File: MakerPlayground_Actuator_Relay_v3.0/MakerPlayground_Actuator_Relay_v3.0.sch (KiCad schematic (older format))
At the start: 7 parts, among them J1 Conn_01x04, J2 Terminal Block, J3 Terminal Block, K1 SANYOU_SRD_Form_C, Q1 Q_NPN_BEC

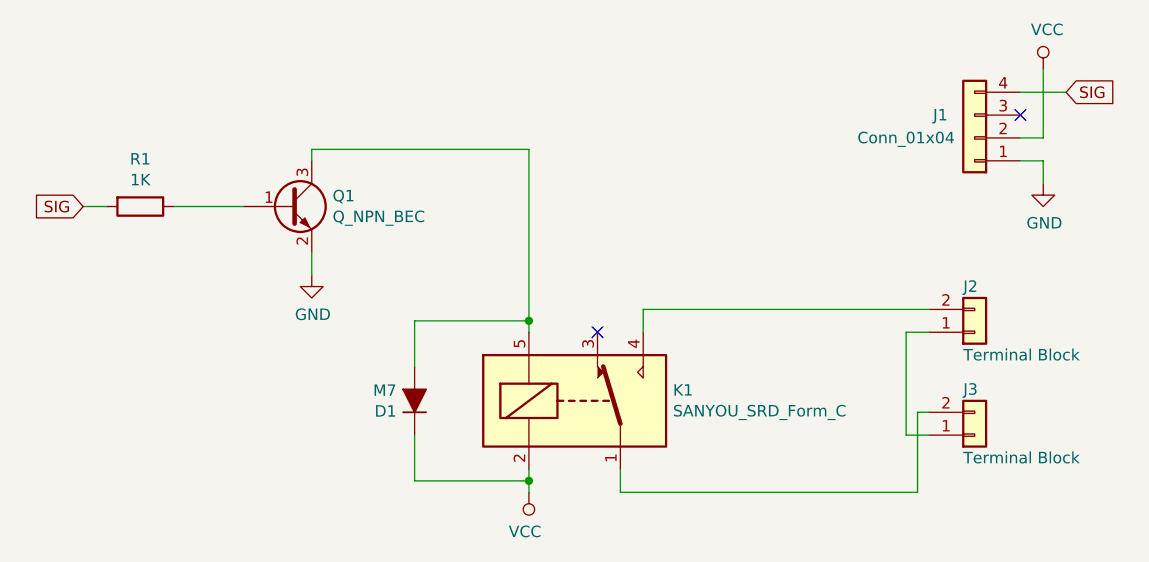
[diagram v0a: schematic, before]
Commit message: Fix wiring error.
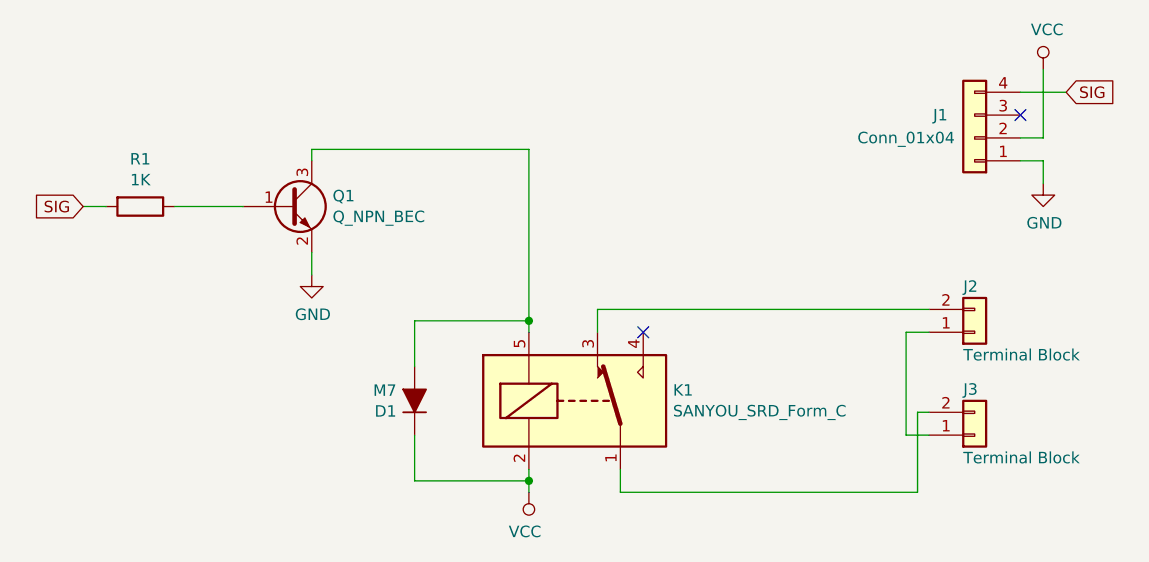
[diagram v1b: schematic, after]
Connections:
- net at K1.3: now also J2.2 (Pin_2)
- net at K1.4: no longer J2.2 (Pin_2)
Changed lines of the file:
@@
 EESchema Schematic File Version 4
+LIBS:MakerPlayground_Actuator_Relay_v3.0-cache
 EELAYER 26 0
 EELAYER END
@@
 Wire Wire Line
 	4050 3400 4050 3500
-NoConn ~ 3950 2800
 Wire Wire Line
 	4050 3500 5350 3500
-Wire Wire Line
-	4150 2700 4150 2800
 Wire Wire Line
 	2700 2050 2700 2000
@@
 	5350 3150 5350 3500
 Wire Wire Line
-	4150 2700 5400 2700
-Wire Wire Line
 	5400 3250 5300 3250
 Wire Wire Line
@@
 Wire Wire Line
 	5300 2800 5400 2800
+Wire Wire Line
+	3950 2700 3950 2800
+Wire Wire Line
+	3950 2700 5400 2700
+NoConn ~ 4150 2800
 $EndSCHEMATC
